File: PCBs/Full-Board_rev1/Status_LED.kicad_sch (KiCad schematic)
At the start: 2 parts

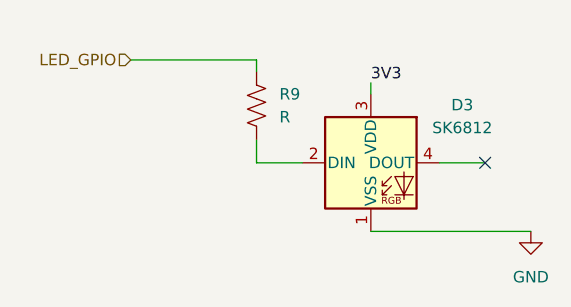
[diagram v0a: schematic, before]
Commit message: Fixed some rules checker errors
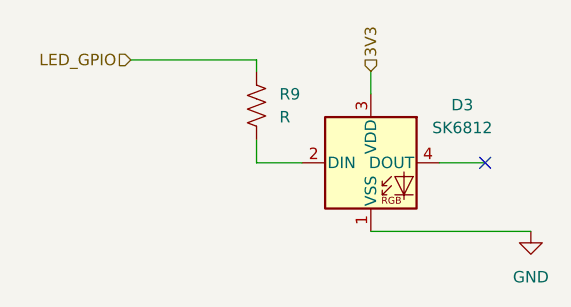
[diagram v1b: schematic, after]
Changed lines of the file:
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@@
 	(wire
 		(pts
-			(xy 149.86 96.52) (xy 149.86 97.79)
+			(xy 149.86 95.25) (xy 149.86 97.79)
 		)
 		(stroke
@@
 		)
 	)
-	(label "3V3"
-		(at 149.86 96.52 0)
+	(hierarchical_label "3V3"
+		(shape input)
+		(at 149.86 95.25 90)
 		(effects
 			(font
 				(size 1.27 1.27)
 			)
-			(justify left bottom)
+			(justify left)
 		)
 	)

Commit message: Added footprints for main board components
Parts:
- R9: footprint (none) -> Connector_PinHeader_2.54mm:PinHeader_1x02_P2.54mm_Vertical
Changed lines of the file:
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@@
 			)
 		)
-		(property "Footprint" ""
+		(property "Footprint" "Connector_PinHeader_2.54mm:PinHeader_1x02_P2.54mm_Vertical"
 			(at 138.176 99.314 90)
 			(effects

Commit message: Redid some faulty footprint assignments
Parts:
- R9: footprint Connector_PinHeader_2.54mm:PinHeader_1x02_P2.54mm_Vertical -> Resistor_THT:R_Axial_DIN0207_L6.3mm_D2.5mm_P2.54mm_Vertical
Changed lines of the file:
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@@
 			)
 		)
-		(property "Footprint" "Connector_PinHeader_2.54mm:PinHeader_1x02_P2.54mm_Vertical"
+		(property "Footprint" "Resistor_THT:R_Axial_DIN0207_L6.3mm_D2.5mm_P2.54mm_Vertical"
 			(at 138.176 99.314 90)
 			(effects

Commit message: Full Board PCB Design Rev1.0 complete
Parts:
- renumbered D3 to D2, R9 to R1
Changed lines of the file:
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@@
 		(dnp no)
 		(fields_autoplaced yes)
-		(property "Reference" "D3"
+		(property "Reference" "D2"
 			(at 160.02 98.9898 0)
 			(effects
@@
 			(project "Full-Board_rev1"
 				(path "/2dd686ed-aa28-474a-bf3c-628eebb4b373/aaa2f8fc-778c-45ba-a467-bd9b333b5317"
-					(reference "D3")
+					(reference "D2")
 					(unit 1)
 				)
@@
 		)
 		(instances
-			(project "Full-Board_rev1"
+			(project ""
 				(path "/2dd686ed-aa28-474a-bf3c-628eebb4b373/aaa2f8fc-778c-45ba-a467-bd9b333b5317"
 					(reference "#PWR014")
@@
 		(dnp no)
 		(fields_autoplaced yes)
-		(property "Reference" "R9"
+		(property "Reference" "R1"
 			(at 139.7 97.7899 0)
 			(effects
@@
 			(project "Full-Board_rev1"
 				(path "/2dd686ed-aa28-474a-bf3c-628eebb4b373/aaa2f8fc-778c-45ba-a467-bd9b333b5317"
-					(reference "R9")
+					(reference "R1")
 					(unit 1)
 				)

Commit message: restructured main layout, needs some cleanup still
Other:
- title: (none) -> SwarmSolve PCB
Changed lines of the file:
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@@
 	(generator_version "9.0")
 	(paper "A4")
+	(title_block
+		(title "SwarmSolve PCB")
+		(date "2025-08-26")
+		(rev "1")
+	)
 	(no_connect
 		(at 162.56 105.41)
